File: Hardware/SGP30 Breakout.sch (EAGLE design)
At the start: 28 parts, among them J3 PTH, Q1 MOSFET-NCH-BSS138, Q2 MOSFET-NCH-BSS138, U1 SGP30, U2 AP2112K

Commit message: pre-review changes
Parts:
- removed J3: PTH, SparkX:I2C_STANDARD_NO_SILK
- added I2C: JUMPER-SMT_3_2-NC_TRACE_SILK, SparkFun-Jumpers:JUMPER-SMT_3_2-NC_TRACE_SILK
- added J1: (no value), SparkFun-Connectors:CONN_041X04_NO_SILK
- J2, J4: value (none) -> QWIIC_RIGHT_ANGLE
- Q1, Q2: value MOSFET-NCH-BSS138 -> 220mA/50V/3.5Ω
- renumbered U1 to U3
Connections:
- new net N$2: I2C.3, R1.2
- new net N$4: I2C.1, R7.2
- net 3.3V: now also I2C.2, J1.2; no longer J3.VCC, R1.2, R7.2
- net GND: now also J1.1; no longer J3.GND
- net SCL: now also J1.4; no longer J3.SCL
- net SDA: now also J1.3; no longer J3.SDA
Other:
- note added: "Cut I2C Jumper to remove pullup resistors from the I2C bus"
- note added: "VIN: 2.5-6.0V"

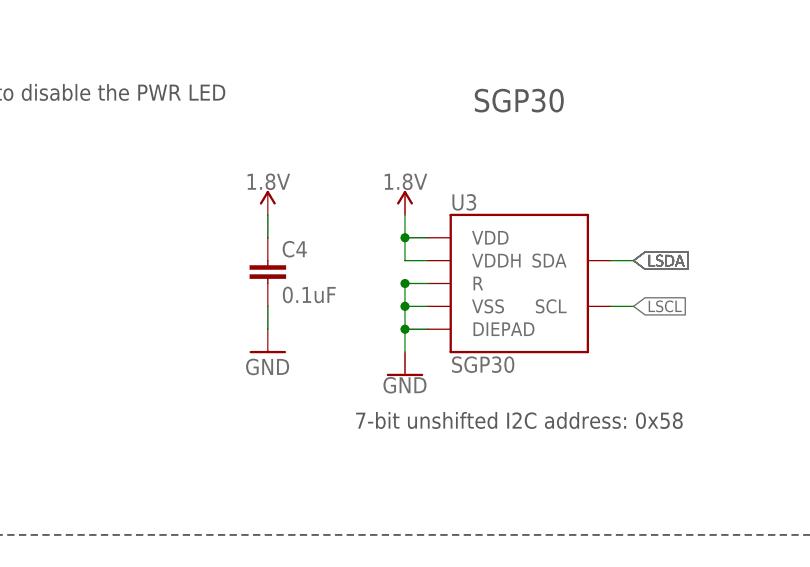
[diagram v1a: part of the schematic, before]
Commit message: Post review/checklist changes
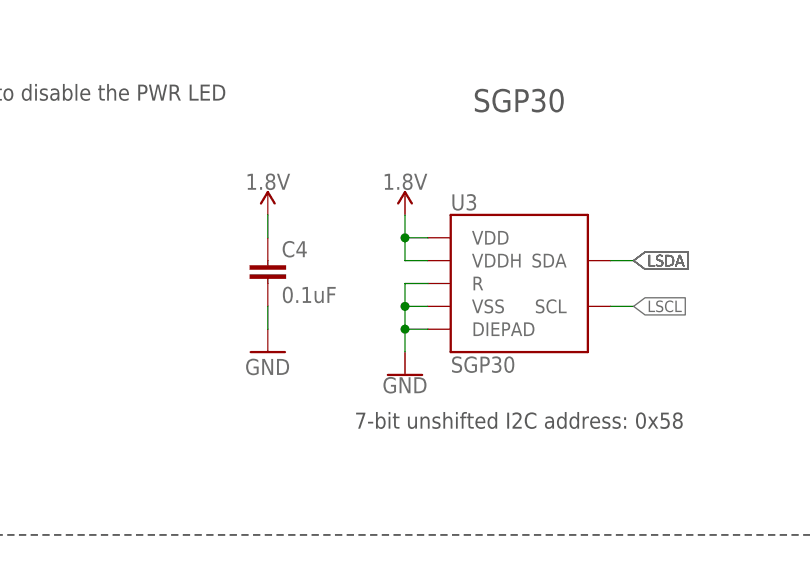
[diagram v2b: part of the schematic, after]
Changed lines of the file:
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@@
 <wire x1="109.22" y1="91.44" x2="109.22" y2="88.9" width="0.1524" layer="91"/>
 <wire x1="111.76" y1="96.52" x2="109.22" y2="96.52" width="0.1524" layer="91"/>
-<junction x="109.22" y="96.52"/>
 <wire x1="111.76" y1="91.44" x2="109.22" y2="91.44" width="0.1524" layer="91"/>
 <junction x="109.22" y="91.44"/>

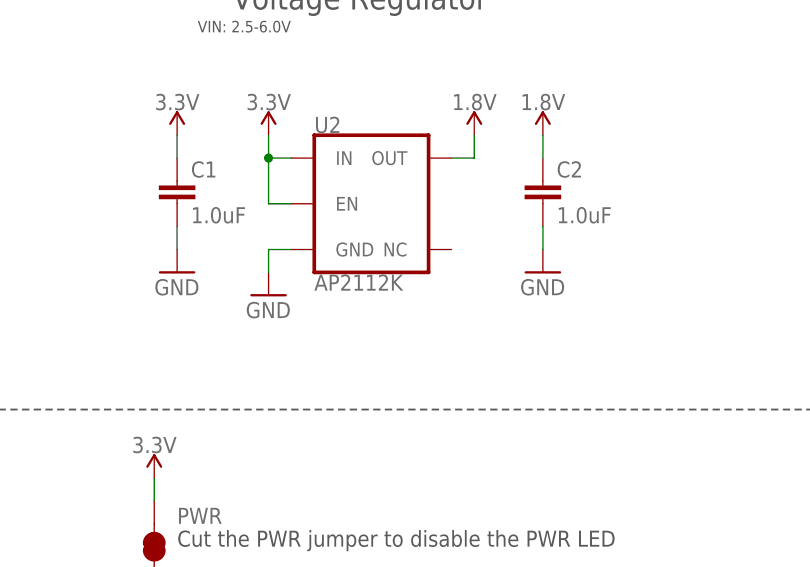
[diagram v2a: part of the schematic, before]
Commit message: replacing 3.3V VREG with 1.8V in Schematic
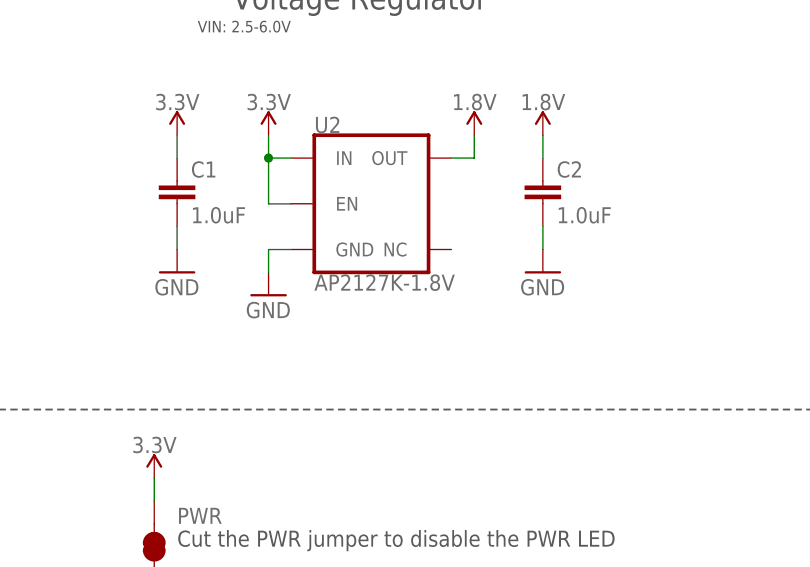
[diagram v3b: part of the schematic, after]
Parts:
- U2: value AP2112K -> AP2127K-1.8V; device SparkFun-IC-Power:V_REG_AP2112K-3.3V -> SparkFun-IC-Power:V_REG_AP2127K-1.8V
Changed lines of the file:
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@@
 <part name="SUPPLY3" library="SparkFun-PowerSymbols" deviceset="3.3V" device=""/>
 <part name="SUPPLY5" library="SparkFun-PowerSymbols" deviceset="1.8V" device=""/>
-<part name="U2" library="SparkFun-IC-Power" deviceset="V_REG_AP2112" device="K-3.3V" value="AP2112K"/>
+<part name="U2" library="SparkFun-IC-Power" deviceset="V_REG_AP2127" device="K-1.8V" value="AP2127K-1.8V"/>
 <part name="GND2" library="SparkFun" deviceset="GND" device=""/>
 <part name="Q1" library="SparkFun-DiscreteSemi" deviceset="MOSFET-NCH" device="-BSS138" value="220mA/50V/3.5Ω"/>
